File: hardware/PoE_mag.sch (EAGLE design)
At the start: 126 parts, among them IC1 LD1117V33, IC10 74LVC1T45SOT23-HAND, IC11 74LVC1T45SOT23-HAND, IC12 PCA9517A, IC2 LD1117V33, IC3 DS1338, IC4 ATMEGA1284, IC5 TSR 1-2450, IC6 LM61, IC7 MCP2200, IC8 74LVC1T45SOT23-HAND, IC9 74LVC1T45SOT23-HAND, Q1 BSS138, Q2 BUK98150-55A, X1 PWR, X2 JTAG, X3 USB, X4 MICRO-SD-SOCKETHIROSE-DM3D, X5 CONN-SMATHD, X6 UFL, X7 22-23-2021, X8 RJ45, X9 RJ11, Y1 32k768, Y2 16MHz, Y3 12MHz

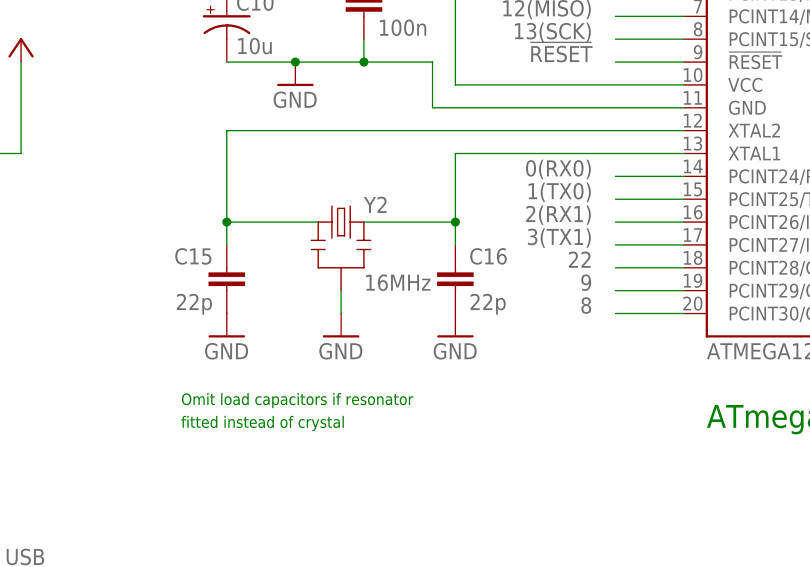
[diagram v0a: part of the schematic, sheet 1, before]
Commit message: Update crystal value
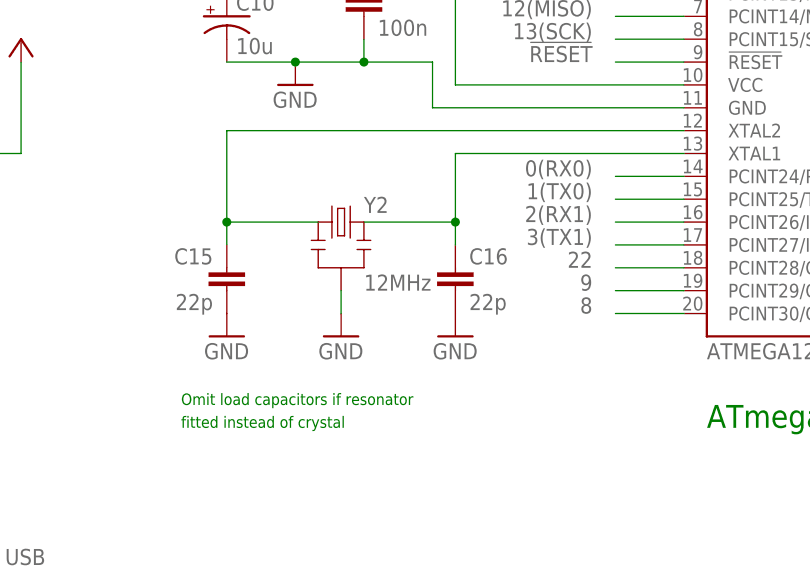
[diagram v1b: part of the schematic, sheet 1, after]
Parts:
- Y2: value 16MHz -> 12MHz
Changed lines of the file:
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@@
 <part name="+3V1" library="supply1" deviceset="+3V3" device=""/>
 <part name="P+14" library="supply1" deviceset="+5V" device=""/>
-<part name="Y2" library="SteveMarple" deviceset="CRYSTAL-RESONATOR" device="" value="16MHz">
+<part name="Y2" library="SteveMarple" deviceset="CRYSTAL-RESONATOR" device="" value="12MHz">
 <attribute name="OPTION" value="Crystal or ceramic resonator. Max 12MHz for 3V3 operation."/>
 </part>

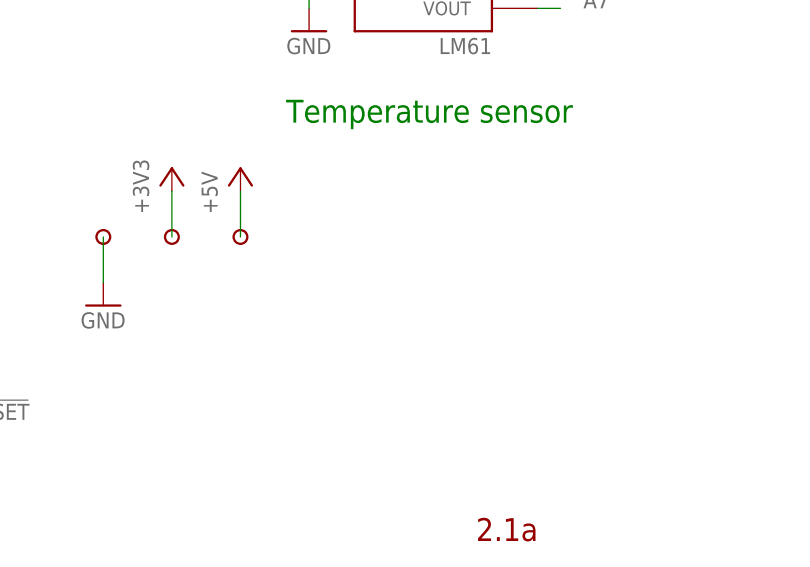
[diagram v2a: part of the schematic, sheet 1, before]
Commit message: Add pads for support wire over 32768Hz crystal
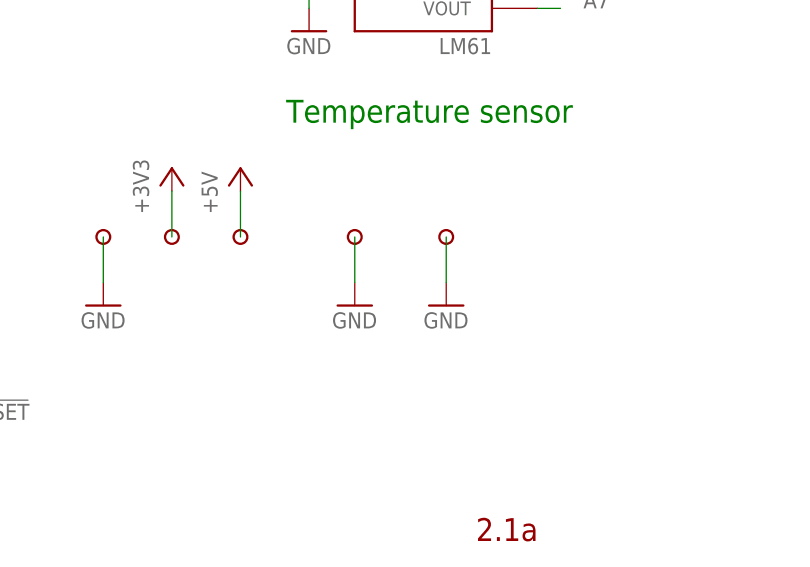
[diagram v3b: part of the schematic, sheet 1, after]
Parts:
- added U$14, U$15: PAD, SteveMarple:PAD
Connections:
- net GND: now also U$14.1, U$15.1
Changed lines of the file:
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@@
 <part name="C12" library="SteveMarple" deviceset="CAP_POL" device="" value="100u 25V"/>
 <part name="C14" library="SteveMarple" deviceset="CAP_POL" device="100UF-16V-100MIL" value="100u"/>
+<part name="U$14" library="SteveMarple" deviceset="PAD" device=""/>
+<part name="GND50" library="supply1" deviceset="GND" device=""/>
+<part name="U$15" library="SteveMarple" deviceset="PAD" device=""/>
+<part name="GND51" library="supply1" deviceset="GND" device=""/>
 </parts>
 <sheets>
@@
 </instance>
 <instance part="C14" gate="G$1" x="-111.76" y="22.86"/>
+<instance part="U$14" gate="G$1" x="142.24" y="-27.94"/>
+<instance part="GND50" gate="1" x="142.24" y="-35.56"/>
+<instance part="U$15" gate="G$1" x="152.4" y="-27.94"/>
+<instance part="GND51" gate="1" x="152.4" y="-35.56"/>
 </instances>
 <busses>
@@
 <pinref part="GND49" gate="1" pin="GND"/>
 </segment>
+<segment>
+<pinref part="U$14" gate="G$1" pin="1"/>
+<pinref part="GND50" gate="1" pin="GND"/>
+<wire x1="142.24" y1="-33.02" x2="142.24" y2="-27.94" width="0.1524" layer="91"/>
+</segment>
+<segment>
+<pinref part="U$15" gate="G$1" pin="1"/>
+<pinref part="GND51" gate="1" pin="GND"/>
+<wire x1="152.4" y1="-33.02" x2="152.4" y2="-27.94" width="0.1524" layer="91"/>
+</segment>
 </net>

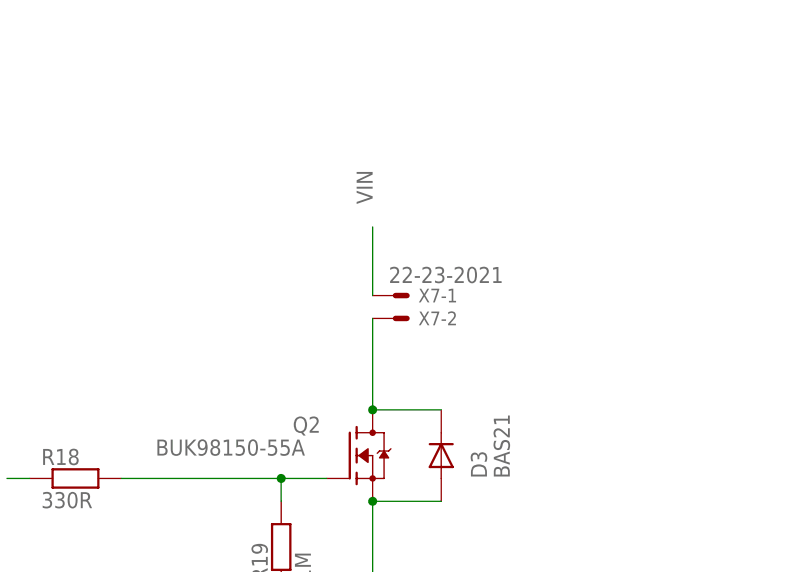
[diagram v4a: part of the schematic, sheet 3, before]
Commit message: Add cap for RFI suppression across fan, minor track layout changes
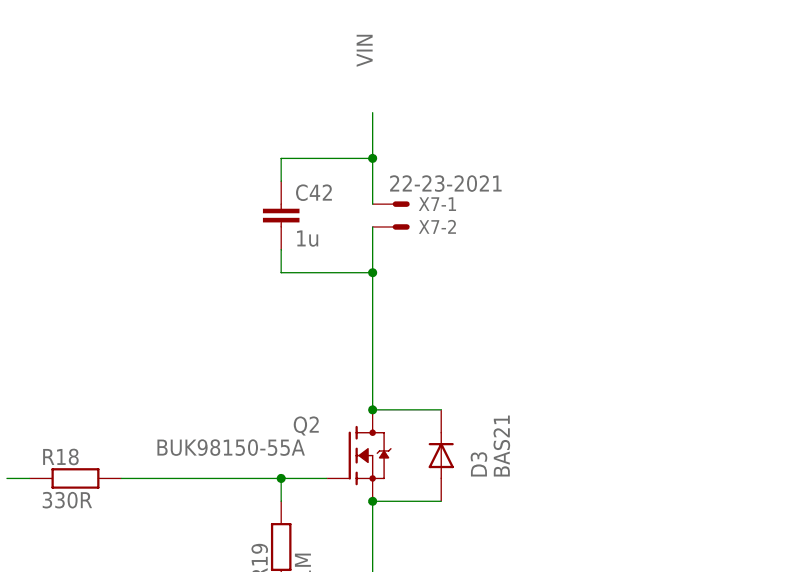
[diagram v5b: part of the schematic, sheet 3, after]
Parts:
- added C42: 1u, SteveMarple:C-EU1206-HAND
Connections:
- net FAN_CTRL: now also C42.2
- net VIN: now also C42.1
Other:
- moved on the sheet: X7-1, X7-2
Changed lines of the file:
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@@
 <part name="U$15" library="SteveMarple" deviceset="PAD" device=""/>
 <part name="GND51" library="supply1" deviceset="GND" device=""/>
+<part name="C42" library="SteveMarple" deviceset="C-EU" device="1206-HAND" value="1u"/>
 </parts>
 <sheets>
@@
 <instance part="D3" gate="G$1" x="106.68" y="182.88" rot="R90"/>
 <instance part="GND48" gate="1" x="88.9" y="165.1"/>
-<instance part="X7" gate="-1" x="101.6" y="200.66"/>
-<instance part="X7" gate="-2" x="101.6" y="198.12"/>
+<instance part="X7" gate="-1" x="101.6" y="210.82"/>
+<instance part="X7" gate="-2" x="101.6" y="208.28"/>
 <instance part="BOX1" gate="G$1" x="337.82" y="53.34"/>
 <instance part="Q2" gate="G$1" x="99.06" y="182.88" smashed="yes">
@@
 <instance part="D4" gate="G$1" x="58.42" y="66.04" rot="R90"/>
 <instance part="P+19" gate="VCC" x="58.42" y="81.28"/>
+<instance part="C42" gate="G$1" x="88.9" y="210.82"/>
 </instances>
 <busses>
@@
 </segment>
 </net>
-<net name="FAN_CTRL" class="0">
+<net name="FAN_CTRL" class="1">
 <segment>
 <junction x="99.06" y="187.96"/>
-<wire x1="99.06" y1="187.96" x2="99.06" y2="198.12" width="0.1524" layer="91"/>
+<wire x1="99.06" y1="187.96" x2="99.06" y2="203.2" width="0.1524" layer="91"/>
 <pinref part="D3" gate="G$1" pin="C"/>
+<wire x1="99.06" y1="203.2" x2="99.06" y2="208.28" width="0.1524" layer="91"/>
 <wire x1="106.68" y1="187.96" x2="99.06" y2="187.96" width="0.1524" layer="91"/>
 <pinref part="X7" gate="-2" pin="S"/>
 <pinref part="Q2" gate="G$1" pin="D"/>
+<junction x="99.06" y="203.2"/>
+<pinref part="C42" gate="G$1" pin="2"/>
+<wire x1="88.9" y1="205.74" x2="88.9" y2="203.2" width="0.1524" layer="91"/>
+<wire x1="88.9" y1="203.2" x2="99.06" y2="203.2" width="0.1524" layer="91"/>
 </segment>
 </net>
@@
 <segment>
 <pinref part="X7" gate="-1" pin="S"/>
-<wire x1="99.06" y1="200.66" x2="99.06" y2="208.28" width="0.1524" layer="91"/>
-<label x="99.06" y="210.82" size="1.778" layer="95" rot="R90"/>
-</segment>
-<segment>
+<wire x1="99.06" y1="210.82" x2="99.06" y2="215.9" width="0.1524" layer="91"/>
+<label x="99.06" y="226.06" size="1.778" layer="95" rot="R90"/>
+<junction x="99.06" y="215.9"/>
+<wire x1="99.06" y1="215.9" x2="99.06" y2="220.98" width="0.1524" layer="91"/>
+<pinref part="C42" gate="G$1" pin="1"/>
+<wire x1="88.9" y1="213.36" x2="88.9" y2="215.9" width="0.1524" layer="91"/>
+<wire x1="88.9" y1="215.9" x2="99.06" y2="215.9" width="0.1524" layer="91"/>
+</segment>
+<segment>
